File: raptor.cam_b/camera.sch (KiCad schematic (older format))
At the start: 3 parts, among them P1 CONN_01X15, P2 CONN_01X05, P3 CONN_01X16

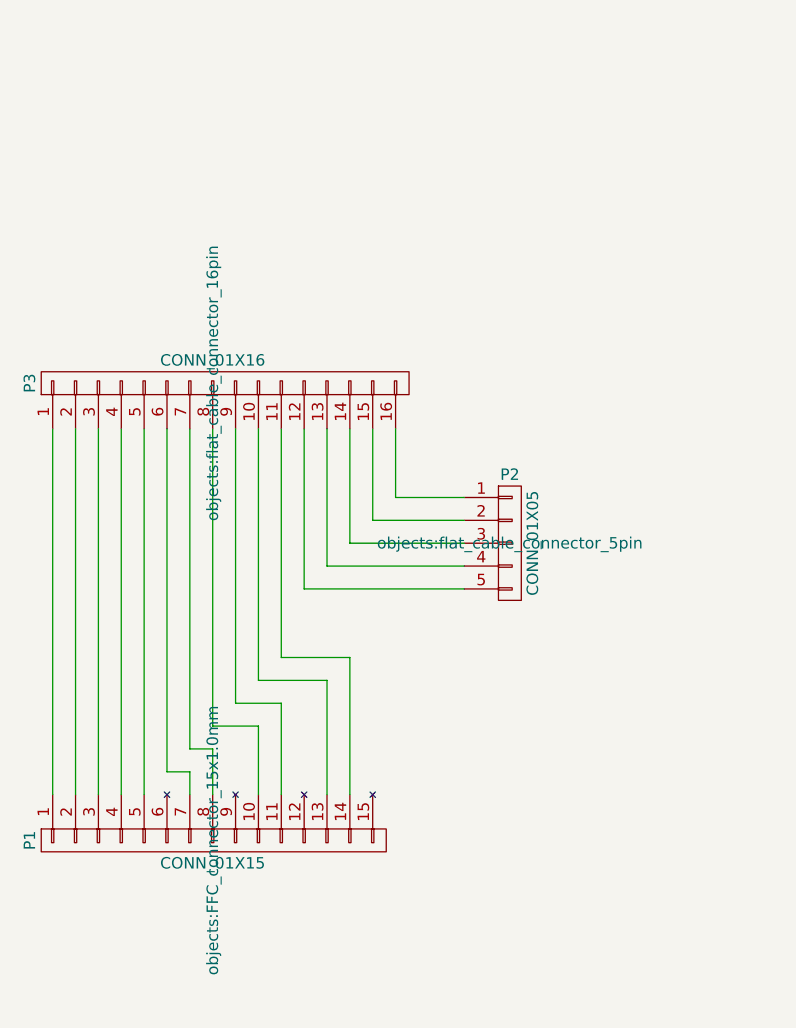
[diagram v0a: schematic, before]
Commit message: Dodaję adapter na przejścia do taśmy.
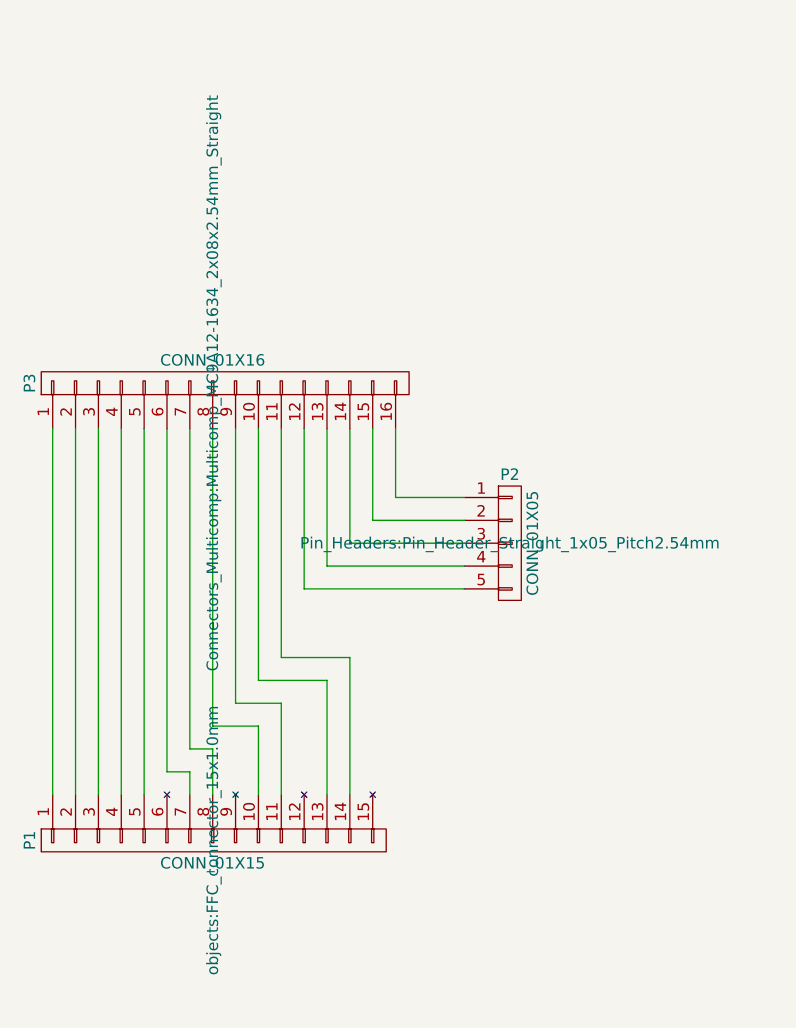
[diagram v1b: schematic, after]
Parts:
- P2: footprint objects:flat_cable_connector_5pin -> Pin_Headers:Pin_Header_Straight_1x05_Pitch2.54mm
- P3: footprint objects:flat_cable_connector_16pin -> Connectors_Multicomp:Multicomp_MC9A12-1634_2x08x2.54mm_Straight
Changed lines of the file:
@@
 F 0 "P2" H 7300 3500 50  0000 C CNN
 F 1 "CONN_01X05" V 7400 3200 50  0000 C CNN
-F 2 "objects:flat_cable_connector_5pin" H 7300 3200 50  0000 C CNN
+F 2 "Pin_Headers:Pin_Header_Straight_1x05_Pitch2.54mm" H 7300 3200 50  0000 C CNN
 F 3 "" H 7300 3200 50  0000 C CNN
 	1    7300 3200
@@
 F 0 "P3" V 5200 2900 50  0000 C CNN
 F 1 "CONN_01X16" H 6000 3000 50  0000 C CNN
-F 2 "objects:flat_cable_connector_16pin" V 6000 2900 50  0000 C CNN
+F 2 "Connectors_Multicomp:Multicomp_MC9A12-1634_2x08x2.54mm_Straight" V 6000 2900 50  0000 C CNN
 F 3 "" V 6000 2900 50  0000 C CNN
 	1    6000 2700

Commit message: Opracowałem płytkę na złącze pcb taśmy.
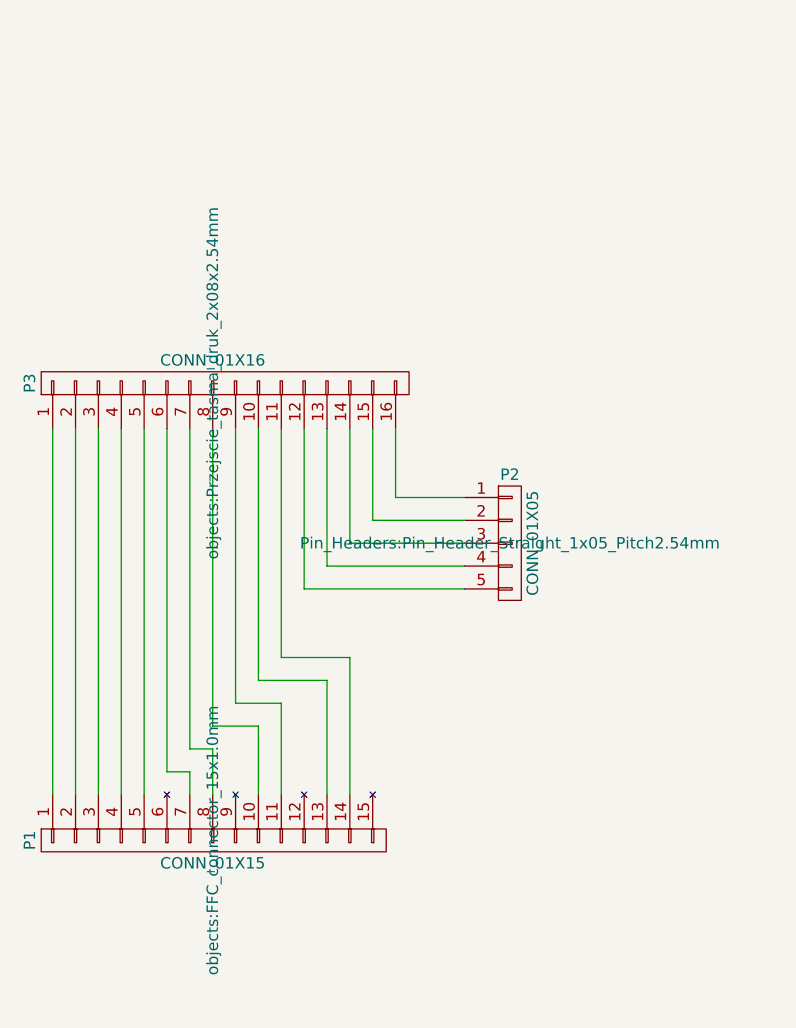
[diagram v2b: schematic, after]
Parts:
- P3: footprint Connectors_Multicomp:Multicomp_MC9A12-1634_2x08x2.54mm_Straight -> objects:Przejscie_tasma_druk_2x08x2.54mm
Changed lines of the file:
@@
 F 0 "P3" V 5200 2900 50  0000 C CNN
 F 1 "CONN_01X16" H 6000 3000 50  0000 C CNN
-F 2 "Connectors_Multicomp:Multicomp_MC9A12-1634_2x08x2.54mm_Straight" V 6000 2900 50  0000 C CNN
+F 2 "objects:Przejscie_tasma_druk_2x08x2.54mm" V 6000 2900 50  0000 C CNN
 F 3 "" V 6000 2900 50  0000 C CNN
 	1    6000 2700

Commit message: Prace nad płytką cd.
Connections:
- net at P2.2 (P2): now also P3.14 (P14); no longer P3.15 (P15)
- net at P2.3 (P3): now also P3.12 (P12); no longer P3.14 (P14)
- net at P2.4 (P4): now also P3.10 (P10); no longer P3.13 (P13)
- net at P2.5 (P5): now also P3.8 (P8); no longer P3.12 (P12)
- net at P1.1 (P1), P3.1 (P1): now also P1.4 (P4), P3.6 (P6)
- net at P1.10 (P10): now also P3.9 (P9); no longer P3.8 (P8)
- net at P1.11 (P11): now also P3.11 (P11); no longer P3.9 (P9)
- net at P1.13 (P13): now also P3.13 (P13); no longer P3.10 (P10)
- net at P1.14 (P14): now also P3.15 (P15); no longer P3.11 (P11)
- net at P1.2 (P2): now also P3.4 (P4); no longer P3.2 (P2)
- net at P1.3 (P3), P3.3 (P3): now also P1.5 (P5), P3.2 (P2)
- net at P3.5 (P5): now also P1.7 (P7); no longer P1.5 (P5)
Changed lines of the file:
@@
 $EndComp
 Wire Wire Line
-	5300 4300 5300 2700
+	6400 3200 7100 3200
 Wire Wire Line
-	5400 4300 5400 2700
+	7100 3000 6800 3000
 Wire Wire Line
-	5500 4300 5500 2700
+	6800 3000 6800 2700
 Wire Wire Line
-	5600 4300 5600 2700
+	7100 3100 6600 3100
 Wire Wire Line
-	5700 4300 5700 2700
+	6600 3100 6600 2700
 Wire Wire Line
-	5900 4300 5900 4200
+	6400 3200 6400 2700
 Wire Wire Line
-	5900 4200 5800 4200
+	7100 3300 6200 3300
 Wire Wire Line
-	5800 4200 5800 2700
+	6200 3300 6200 2700
 Wire Wire Line
-	6000 4300 6000 4100
+	7100 3400 6000 3400
 Wire Wire Line
-	6000 4100 5900 4100
+	6000 3400 6000 2700
 Wire Wire Line
-	5900 4100 5900 2700
+	6600 4300 6600 4200
 Wire Wire Line
-	6200 4300 6200 4000
+	6600 4200 6700 4200
 Wire Wire Line
-	6200 4000 6000 4000
+	6700 4200 6700 2700
 Wire Wire Line
-	6000 4000 6000 2700
+	6500 4300 6500 2700
 Wire Wire Line
-	6300 4300 6300 3900
+	6300 4300 6300 2700
 Wire Wire Line
-	6300 3900 6100 3900
+	6200 4300 6200 3500
 Wire Wire Line
-	6100 3900 6100 2700
+	6200 3500 6100 3500
 Wire Wire Line
-	6500 4300 6500 3800
+	6100 3500 6100 2700
 Wire Wire Line
-	6500 3800 6200 3800
+	6000 4300 6000 3500
 Wire Wire Line
-	6200 3800 6200 2700
+	6000 3500 5900 3500
 Wire Wire Line
-	6600 4300 6600 3700
+	5900 3500 5900 2700
 Wire Wire Line
-	6600 3700 6300 3700
+	5900 4300 5900 3600
 Wire Wire Line
-	6300 3700 6300 2700
+	5900 3600 5700 3600
 Wire Wire Line
-	6400 2700 6400 3400
+	5700 3600 5700 2700
 Wire Wire Line
-	6400 3400 7100 3400
+	5700 4300 5700 3800
 Wire Wire Line
-	6500 2700 6500 3300
+	5700 3800 5500 3800
 Wire Wire Line
-	6500 3300 7100 3300
+	5500 3800 5500 2700
 Wire Wire Line
-	6600 2700 6600 3200
+	5600 4300 5600 4000
 Wire Wire Line
-	6600 3200 7100 3200
+	5600 4000 5300 4000
 Wire Wire Line
-	6700 2700 6700 3100
+	5300 4000 5300 2700
 Wire Wire Line
-	6700 3100 7100 3100
+	5300 4300 5300 3400
 Wire Wire Line
-	6800 2700 6800 3000
+	5300 3400 5800 3400
 Wire Wire Line
-	6800 3000 7100 3000
+	5800 3400 5800 2700
+Wire Wire Line
+	5400 4300 5400 3900
+Wire Wire Line
+	5400 3900 5600 3900
+Wire Wire Line
+	5600 3900 5600 2700
+Wire Wire Line
+	5500 4300 5500 3700
+Wire Wire Line
+	5500 3700 5400 3700
+Wire Wire Line
+	5400 3700 5400 2700
 $EndSCHEMATC
